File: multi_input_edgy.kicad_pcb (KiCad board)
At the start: 2 copper layers, 60 x 43.2 mm, 84 parts, among them J1 002, J2 002, J3 In1, J4 In2, J5 In3, J6 In4, J7 6V-24V, Q1 PMV213SN, Q10 DMP610DL, Q11 2N7002, Q12 2N7002, Q13 PMV213SN, Q14 DMP610DL, Q15 2N7002, Q16 2N7002, Q2 DMP610DL, Q3 2N7002, Q4 2N7002, Q5 PMV213SN, Q6 DMP610DL, Q7 2N7002, Q8 2N7002, Q9 PMV213SN, U1 EL3H7, U10 AL5809, U11 EL3H7, U12 EL3H7, U13 AL5809, U14 AL5809, U15 EL3H7, U16 EL3H7, U17 HEF4021BT, U18 SN74LVC1G125, U2 AL5809, U3 AL5809, U4 EL3H7, U5 AL5809, U6 AL5809, U7 EL3H7, U8 EL3H7, U9 AL5809

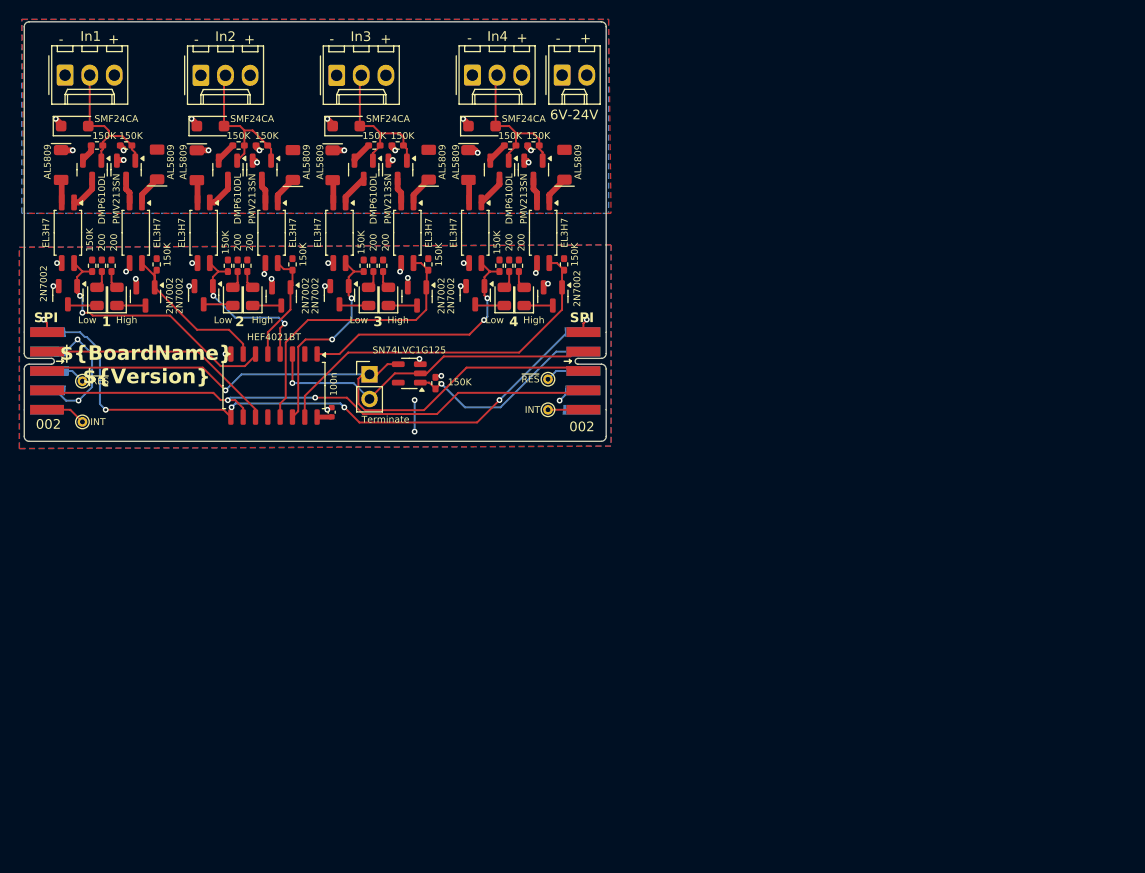
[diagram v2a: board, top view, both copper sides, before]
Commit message: Change optocouplers, improve power routing
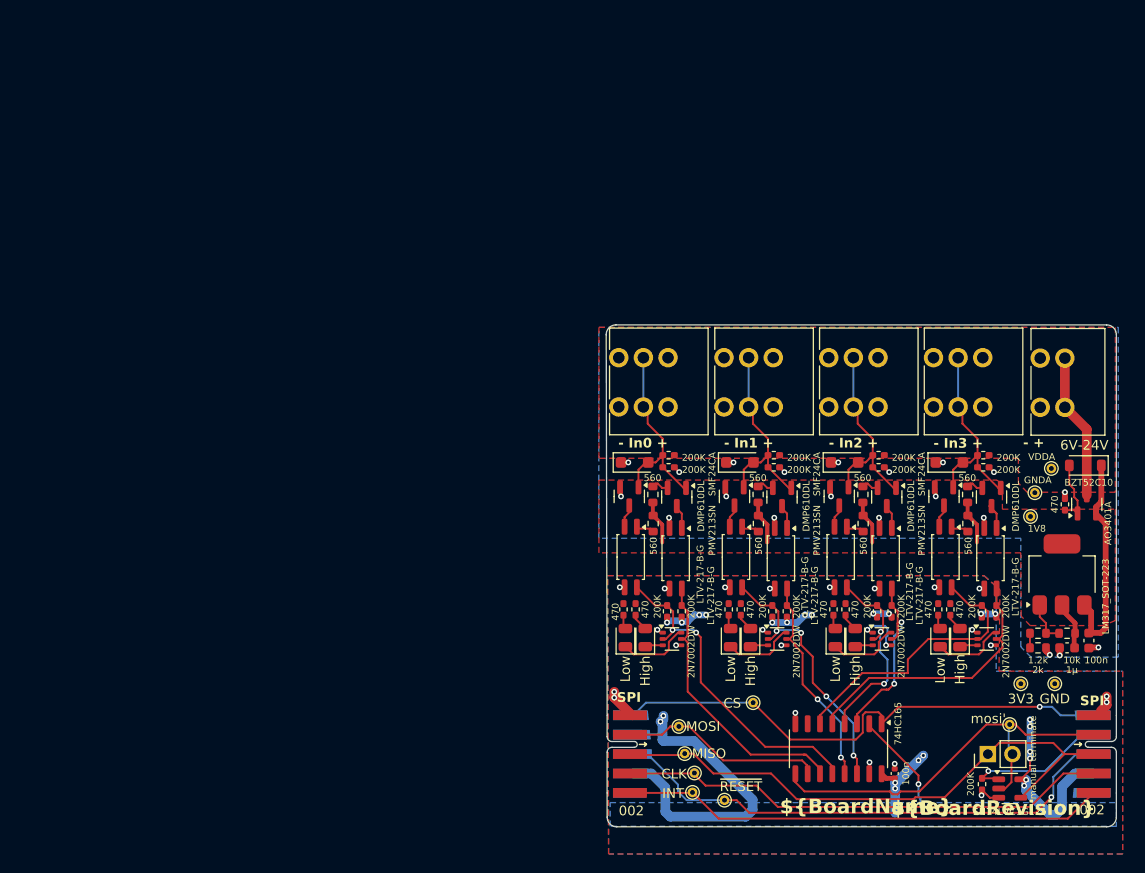
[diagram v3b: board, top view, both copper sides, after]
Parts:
- removed Q12, Q16, Q4, Q8: 2N7002, Package_TO_SOT_SMD:SOT-23
- removed TP1, TP3: INT, TestPoint:TestPoint_THTPad_D1.0mm_Drill0.5mm
- removed TP2, TP4: ~{RES}, TestPoint:TestPoint_THTPad_D1.0mm_Drill0.5mm
- removed U11, U15, U16: EL3H7, lcsc_stuff:SSOP-4_4.4x2.6mm_P1.27mm
- removed U13, U14: AL5809, lcsc_stuff:PowerDI-123
- removed U17: HEF4021BT, Package_SO:SOIC-16_4.55x10.3mm_P1.27mm
- removed U18: SN74LVC1G125, Package_TO_SOT_SMD:SOT-23-5
- added C10: 1µ, Capacitor_SMD:C_0603_1608Metric, F.Cu at (240.5, 99.3)
- added C9: 100n, Capacitor_SMD:C_0603_1608Metric, F.Cu at (242.8, 98.5)
- added D13: BZT52C10, Diode_SMD:D_SOD-123, F.Cu at (242.4, 80.5)
- added Q17: AO3401A, Package_TO_SOT_SMD:SOT-23, F.Cu at (242.6, 84.5)
- added R26: 10k, Resistor_SMD:R_0603_1608Metric, F.Cu at (240.5, 97.8)
- added R27: 1.2k, Resistor_SMD:R_0603_1608Metric, F.Cu at (237.5, 97.8)
- added R28: 470, Resistor_SMD:R_0402_1005Metric_Pad0.72x0.64mm_HandSolder, F.Cu at (240.3, 84.5)
- added R29: 2k, Resistor_SMD:R_0603_1608Metric, F.Cu at (237.5, 99.3)
- added R30: 560, Resistor_SMD:R_0603_1608Metric, F.Cu at (208.7, 86.5)
- added R31: 560, Resistor_SMD:R_0603_1608Metric, F.Cu at (219.5, 86.5)
- added R32: 560, Resistor_SMD:R_0603_1608Metric, F.Cu at (197.8, 86.5)
- added R33: 560, Resistor_SMD:R_0603_1608Metric, F.Cu at (230.3, 86.5)
- added R34: 560, Resistor_SMD:R_0603_1608Metric, F.Cu at (208.7, 83.5)
- added R35: 560, Resistor_SMD:R_0603_1608Metric, F.Cu at (219.5, 83.5)
- added R36: 560, Resistor_SMD:R_0603_1608Metric, F.Cu at (197.8, 83.5)
- added R37: 560, Resistor_SMD:R_0603_1608Metric, F.Cu at (230.3, 83.5)
- added TP10: MISO, TestPoint:TestPoint_THTPad_D1.0mm_Drill0.5mm, F.Cu at (201.1, 110.2)
- added TP11: mosi', TestPoint:TestPoint_THTPad_D1.0mm_Drill0.5mm, F.Cu at (234.6, 107.2)
- added TP12: CS, TestPoint:TestPoint_THTPad_D1.0mm_Drill0.5mm, F.Cu at (208.2, 105.0)
- added TP13: 3V3, TestPoint:TestPoint_THTPad_D1.0mm_Drill0.5mm, F.Cu at (235.8, 103.0)
- added TP14: GND, TestPoint:TestPoint_THTPad_D1.0mm_Drill0.5mm, F.Cu at (239.2, 103.0)
- added TP15: VDDA, TestPoint:TestPoint_THTPad_D1.0mm_Drill0.5mm, F.Cu at (238.9, 80.8)
- added TP16: GNDA, TestPoint:TestPoint_THTPad_D1.0mm_Drill0.5mm, F.Cu at (237.2, 83.3)
- added TP17: 1V8, TestPoint:TestPoint_THTPad_D1.0mm_Drill0.5mm, F.Cu at (236.8, 85.8)
- added TP6: MOSI, TestPoint:TestPoint_THTPad_D1.0mm_Drill0.5mm, F.Cu at (200.5, 107.4)
- added TP7: CLK, TestPoint:TestPoint_THTPad_D1.0mm_Drill0.5mm, F.Cu at (202.1, 112.2)
- added TP8: INT, TestPoint:TestPoint_THTPad_D1.0mm_Drill0.5mm, F.Cu at (201.9, 114.2)
- added TP9: ~{RESET}, TestPoint:TestPoint_THTPad_D1.0mm_Drill0.5mm, F.Cu at (205.2, 115.0)
- D11, D5, D8: value KT-0805G (emerald) Vf=2.8V -> KT-0805Y (orange-red) Vf=2.0V
- D12, D6, D9: value KT-0805Y (orange-red) Vf=2.0V -> KT-0805G (emerald) Vf=2.8V
- J3: value In1 -> - In1 +; footprint Connector_Molex:Molex_KK-254_AE-6410-03A_1x03_P2.54mm_Vertical -> lcsc_stuff:KF141V-2.54-3P
- J4: value In2 -> - In2 +; footprint Connector_Molex:Molex_KK-254_AE-6410-03A_1x03_P2.54mm_Vertical -> lcsc_stuff:KF141V-2.54-3P
- J5: value In3 -> - In0 +; footprint Connector_Molex:Molex_KK-254_AE-6410-03A_1x03_P2.54mm_Vertical -> lcsc_stuff:KF141V-2.54-3P
- J6: value In4 -> - In3 +; footprint Connector_Molex:Molex_KK-254_AE-6410-03A_1x03_P2.54mm_Vertical -> lcsc_stuff:KF141V-2.54-3P
- J7: footprint Connector_Molex:Molex_KK-254_AE-6410-02A_1x02_P2.54mm_Vertical -> lcsc_stuff:KF141V-2.54-2P
- JP1: value Terminate -> manual terminate
- Q11, Q15, Q3, Q7: value 2N7002 -> 2N7002DW; footprint Package_TO_SOT_SMD:SOT-23 -> Package_TO_SOT_SMD:SOT-363_SC-70-6
- R1, R10, R14, R15, R16, R2, R20, R21, R22, R3, R4, R8, R9: value 150K -> 200K
- R11, R17, R23, R5: value 200 -> 200K
- R12, R18, R24, R6: value 200 -> 470
- R13, R19, R25, R7: value 150K -> 470
- U1: value EL3H7 -> SN74LVC1G125; footprint lcsc_stuff:SSOP-4_4.4x2.6mm_P1.27mm -> Package_TO_SOT_SMD:SOT-23-5
- U10, U3, U5, U6, U9: value AL5809 -> LTV-217-B-G; footprint lcsc_stuff:PowerDI-123 -> lcsc_stuff:SSOP-4_4.4x2.6mm_P1.27mm
- U12: value EL3H7 -> LM317_SOT-223; footprint lcsc_stuff:SSOP-4_4.4x2.6mm_P1.27mm -> Package_TO_SOT_SMD:SOT-223-3_TabPin2
- U2: value AL5809 -> 74HC165; footprint lcsc_stuff:PowerDI-123 -> Package_SO:SO-16_3.9x9.9mm_P1.27mm
- U4, U7, U8: value EL3H7 -> LTV-217-B-G
- moved R1 112.5 mm to (231.8, 113.3), turned to -90 degrees
- moved U1 106.8 mm to (234.6, 113.8), turned to 0 degrees
- moved U9 99.3 mm to (228.0, 89.9), turned to -90 degrees
- moved U2 93.2 mm to (216.9, 109.7)
- moved U10 90.8 mm to (232.6, 90.1), turned to -90 degrees
- moved U12 82.4 mm to (240.0, 91.7), turned to 90 degrees
- moved Q3 81.3 mm to (210.6, 98.4), turned to 0 degrees
- moved U4 80.8 mm to (211.0, 90.1)
- moved Q2 78.7 mm to (211.1, 83.7)
- moved R4 78.7 mm to (210.1, 95.5), turned to 90 degrees
- moved R5 78.2 mm to (211.6, 95.5), turned to 90 degrees
- moved D1 76.9 mm to (206.8, 80.2)
- moved J3 76.6 mm to (204.2, 77.3)
- moved Q6 75.8 mm to (221.9, 83.7)
- moved R10 75.8 mm to (220.9, 95.5), turned to 90 degrees
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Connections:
- D1 pad 2: /4xInput/isolated_input/In -> Net-(D1-A2)
- D10 pad 2: /4xInput/isolated_input3/In -> Net-(D10-A2)
- D4 pad 2: /4xInput/isolated_input1/In -> Net-(D4-A2)
- D7 pad 2: /4xInput/isolated_input2/In -> Net-(D7-A2)
- J1 pad 6: /4xInput/~{CS} -> /4xInput/CS
- J2 pad 2: /downstream_mosi -> /MOSI'
- J2 pad 5: Net-(J2-INT) -> Net-(J1-INT)
- J2 pad 6: /4xInput/~{CS} -> /4xInput/CS
- J2 pad 8: Net-(J2-~{RESET}) -> Net-(J1-~{RESET})
- J3 pad 2: /4xInput/isolated_input/In -> Net-(D1-A2)
- J4 pad 2: /4xInput/isolated_input1/In -> Net-(D4-A2)
- J5 pad 2: /4xInput/isolated_input2/In -> Net-(D7-A2)
- J6 pad 2: /4xInput/isolated_input3/In -> Net-(D10-A2)
- J7 pad 2: VDDA -> VDD_EXT
- JP1 pad 2: /downstream_mosi -> /MOSI'
- Q1 pad 1: /4xInput/isolated_input/In -> Net-(D1-A2)
- Q10 pad 1: /4xInput/isolated_input2/In -> Net-(D7-A2)
- Q10 pad 2: VDDA -> Net-(Q10-S)
- Q11 pad 1: /4xInput/isolated_input2/OutHigh -> GND
- Q11 pad 2: GND -> /4xInput/In0/In0_low
- Q11 pad 3: Net-(D8-K) -> Net-(D9-K)
- Q13 pad 1: /4xInput/isolated_input3/In -> Net-(D10-A2)
- Q14 pad 1: /4xInput/isolated_input3/In -> Net-(D10-A2)
- Q14 pad 2: VDDA -> Net-(Q14-S)
- Q15 pad 1: /4xInput/isolated_input3/OutHigh -> GND
- Q15 pad 2: GND -> /4xInput/In3/In3_low
- Q15 pad 3: Net-(D11-K) -> Net-(D12-K)
- Q2 pad 1: /4xInput/isolated_input/In -> Net-(D1-A2)
- Q2 pad 2: VDDA -> Net-(Q2-S)
- Q3 pad 1: /4xInput/isolated_input/OutLow -> GND
- Q3 pad 2: GND -> /4xInput/In1/In1_low
- Q3 pad 3: Net-(D2-K) -> Net-(D3-K)
- Q5 pad 1: /4xInput/isolated_input1/In -> Net-(D4-A2)
- Q6 pad 1: /4xInput/isolated_input1/In -> Net-(D4-A2)
- Q6 pad 2: VDDA -> Net-(Q6-S)
- Q7 pad 1: /4xInput/isolated_input1/OutHigh -> GND
- Q7 pad 2: GND -> /4xInput/In2/In2_low
- Q7 pad 3: Net-(D5-K) -> Net-(D6-K)
- Q9 pad 1: /4xInput/isolated_input2/In -> Net-(D7-A2)
- R1 pad 1: VDDA -> /downstream_status
- R1 pad 2: /4xInput/isolated_input/In -> GND
- R10 pad 2: /4xInput/isolated_input1/OutLow -> /4xInput/In2/In2_low
- R11 pad 2: Net-(D5-A) -> /4xInput/In2/In2_high
- R12 pad 2: Net-(D6-A) -> Net-(D5-A)
- R13 pad 1: VDDA -> +3V3
- R13 pad 2: /4xInput/isolated_input2/In -> Net-(D6-A)
- R14 pad 1: /4xInput/isolated_input2/In -> VDDA
- R14 pad 2: GNDA -> Net-(D7-A2)
- R15 pad 1: +3V3 -> Net-(D7-A2)
- R15 pad 2: /4xInput/isolated_input2/OutHigh -> GNDA
- R16 pad 2: /4xInput/isolated_input2/OutLow -> /4xInput/In0/In0_low
- R17 pad 2: Net-(D8-A) -> /4xInput/In0/In0_high
- R18 pad 2: Net-(D9-A) -> Net-(D8-A)
- R19 pad 1: VDDA -> +3V3
- R19 pad 2: /4xInput/isolated_input3/In -> Net-(D9-A)
- R2 pad 1: /4xInput/isolated_input/In -> VDDA
- R2 pad 2: GNDA -> Net-(D1-A2)
- R20 pad 1: /4xInput/isolated_input3/In -> VDDA
- R20 pad 2: GNDA -> Net-(D10-A2)
- R21 pad 1: +3V3 -> Net-(D10-A2)
- R21 pad 2: /4xInput/isolated_input3/OutHigh -> GNDA
- R22 pad 2: /4xInput/isolated_input3/OutLow -> /4xInput/In3/In3_low
- R23 pad 2: Net-(D11-A) -> /4xInput/In3/In3_high
- R24 pad 2: Net-(D12-A) -> Net-(D11-A)
- R25 pad 1: /downstream_status -> +3V3
- R25 pad 2: GND -> Net-(D12-A)
- R3 pad 1: +3V3 -> Net-(D1-A2)
- R3 pad 2: /4xInput/isolated_input/OutHigh -> GNDA
- R4 pad 2: /4xInput/isolated_input/OutLow -> /4xInput/In1/In1_low
- R5 pad 2: Net-(D3-A) -> /4xInput/In1/In1_high
- R7 pad 1: VDDA -> +3V3
- R7 pad 2: /4xInput/isolated_input1/In -> Net-(D3-A)
- R8 pad 1: /4xInput/isolated_input1/In -> VDDA
- R8 pad 2: GNDA -> Net-(D4-A2)
- R9 pad 1: +3V3 -> Net-(D4-A2)
- R9 pad 2: /4xInput/isolated_input1/OutHigh -> GNDA
- U1 pad 1: Net-(U1-A) -> /downstream_status
- U1 pad 2: Net-(Q1-D) -> /MOSI'
- U1 pad 4: /4xInput/isolated_input/OutHigh -> /upstream_miso
- U10 pad 1: Net-(U10-in) -> Net-(Q14-D)
- U12 pad 1: Net-(Q10-D) -> Net-(U12-ADJ)
- U12 pad 2: Net-(U12-K) -> +1V8
- U12 pad 3: GND -> VDDA
- U2 pad 1: VDDA -> /4xInput/CS
- U2 pad 2: Net-(U1-A) -> /4xInput/CLK
- U3 pad 1: VDDA -> Net-(U3-A)
- U3 pad 2: Net-(U3-Out) -> Net-(Q1-D)
- U4 pad 2: Net-(U4-K) -> GNDA
- U4 pad 4: /4xInput/isolated_input/OutLow -> /4xInput/In1/In1_high
- U5 pad 1: VDDA -> Net-(U5-A)
- U5 pad 2: Net-(U11-A) -> Net-(Q5-D)
- U6 pad 1: VDDA -> Net-(Q6-D)
- U6 pad 2: Net-(U15-A) -> GNDA
- U7 pad 1: Net-(U3-Out) -> Net-(U7-A)
- U7 pad 2: Net-(Q5-D) -> Net-(Q9-D)
- U7 pad 4: /4xInput/isolated_input1/OutHigh -> /4xInput/In0/In0_low
- U8 pad 1: Net-(Q6-D) -> Net-(Q10-D)
- U8 pad 2: Net-(U10-in) -> GNDA
- U8 pad 4: /4xInput/isolated_input1/OutLow -> /4xInput/In0/In0_high
- U9 pad 1: Net-(U4-K) -> Net-(U9-A)
- U9 pad 2: GNDA -> Net-(Q13-D)
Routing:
- net /4xInput/~{CS}: track 67.9 -> 0.00 mm, vias 4 -> 0
- net +3V3: track 22.7 -> 78.7 mm, vias 5 -> 24
- net /4xInput/CS: track 0.00 -> 53.8 mm, vias 0 -> 1
- net Net-(J1-~{RESET}): track 3.83 -> 52.5 mm, vias 0 -> 1
- net Net-(J1-INT): track 4.17 -> 49.7 mm
- net /MOSI': track 0.00 -> 42.6 mm
- net /4xInput/isolated_input3/OutHigh: track 38.4 -> 0.00 mm
- net /downstream_mosi: track 34.2 -> 0.00 mm, vias 1 -> 0
- net /4xInput/In0/In0_low: track 0.00 -> 33.3 mm, vias 0 -> 2
- net +1V8: track 0.00 -> 31.9 mm
- net /4xInput/In0/In0_high: track 0.00 -> 30.9 mm
- net /4xInput/isolated_input2/OutHigh: track 29.8 -> 0.00 mm
- net /4xInput/In3/In3_low: track 0.00 -> 29.4 mm
- net /4xInput/In3/In3_high: track 0.00 -> 28.3 mm
- net /4xInput/In1/In1_low: track 0.00 -> 27.8 mm, vias 0 -> 4
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- added copper zone on F.Cu, net +1V8
- added copper zone on B.Cu, net +3V3
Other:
- board size 60 x 43.2 mm -> 52.6 x 51.8 mm
- board text added: "${BoardName}"
- board text added: "${BoardRevision}"
- board text added: "- +"
- board text removed: "${BoardName} ${Version}"
- board text removed: "+"
- board text removed: "-"
- board text removed: "1"
- board text removed: "2"
- board text removed: "3"
- board text removed: "4"
